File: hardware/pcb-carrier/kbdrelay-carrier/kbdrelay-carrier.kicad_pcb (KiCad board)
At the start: 2 copper layers, 88 x 55 mm, 24 parts, among them J1 UART_KBD, J2 UART_TGT, J3 5V_IN, U1 ESP32-S3-Zero, U2 ESP32-S3-Zero

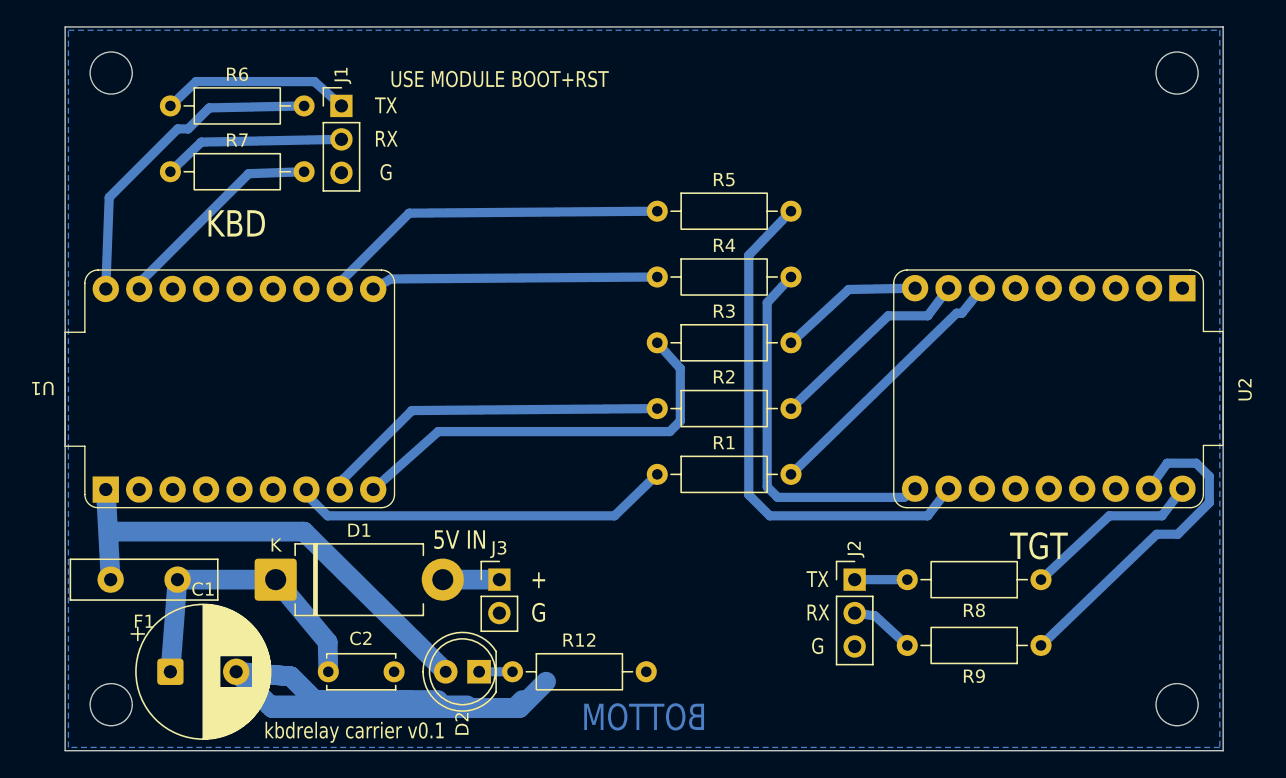
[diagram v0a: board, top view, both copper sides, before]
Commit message: feat(pcb): widen etch tolerance - 0.5 mm routing / 0.8 mm pour clearance
Adds --clearance and --zone-clearance to route.py and raises the defaults.
These are independent: pour clearance is free tolerance (the fill just
retreats, routing is untouched), while routing clearance costs routability.
Both 0.5/0.8 still route with zero jumpers and zero real DRC violations, so
they are the new defaults.

Measured minimum copper gaps on the rebuilt board: pour 0.80 mm, trace-trace
0.70 mm, trace-pad 0.52 mm.

Documents the real constraint: the tightest feature is the 0.54 mm gap between
adjacent module pads, which is fixed geometry (2.54 mm pitch - 2.0 mm pads) and
cannot be improved by any clearance setting. The only lever is shrinking the
module pad to 1.8 mm, trading annular ring for gap.

All fab outputs (Gerbers, drill, 1:1 PDFs, LCD exposure bitmaps) regenerated
against the new routing.
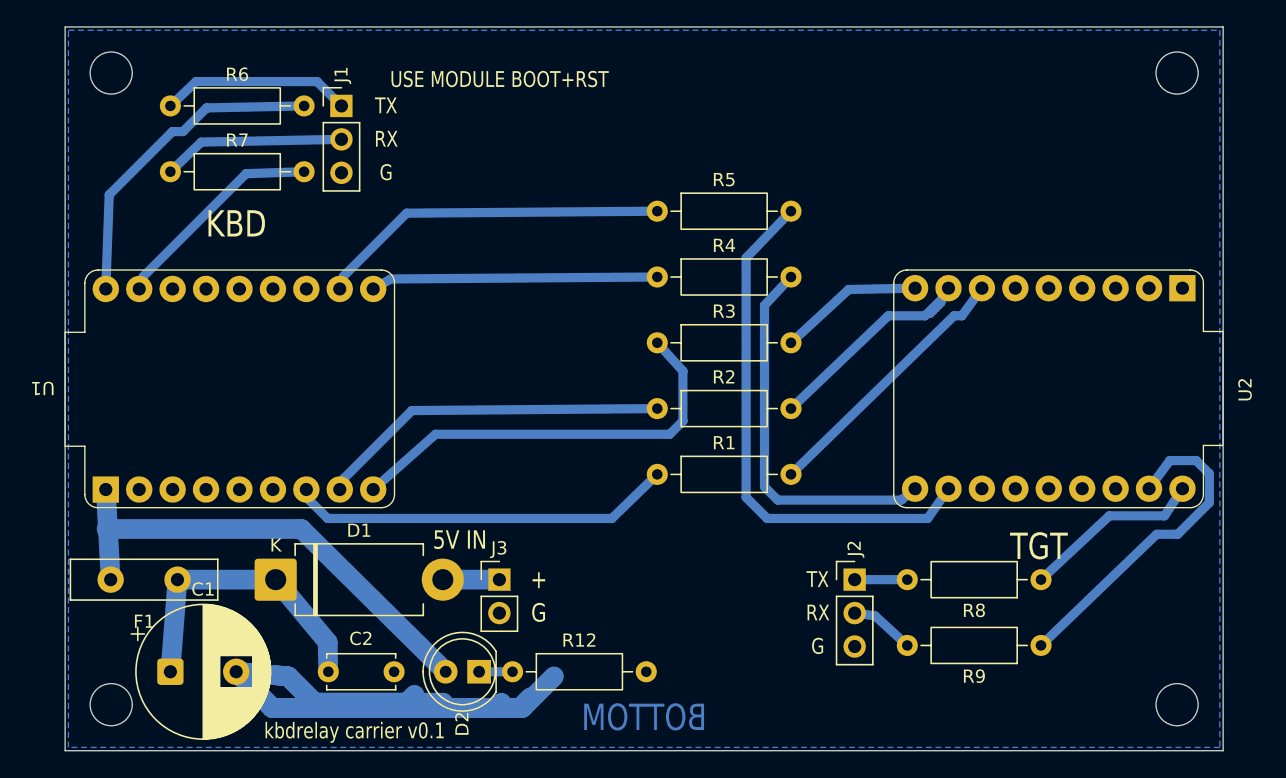
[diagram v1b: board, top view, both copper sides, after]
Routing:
- net GND: track 118.2 -> 121.9 mm
- net /DRDY_TGT: track 39.7 -> 40.3 mm
- net Net-(U2-GPIO5): track 15.8 -> 16.4 mm
